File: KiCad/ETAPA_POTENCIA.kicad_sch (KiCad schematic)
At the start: 7 parts, among them U1 LM1117DT-3.3

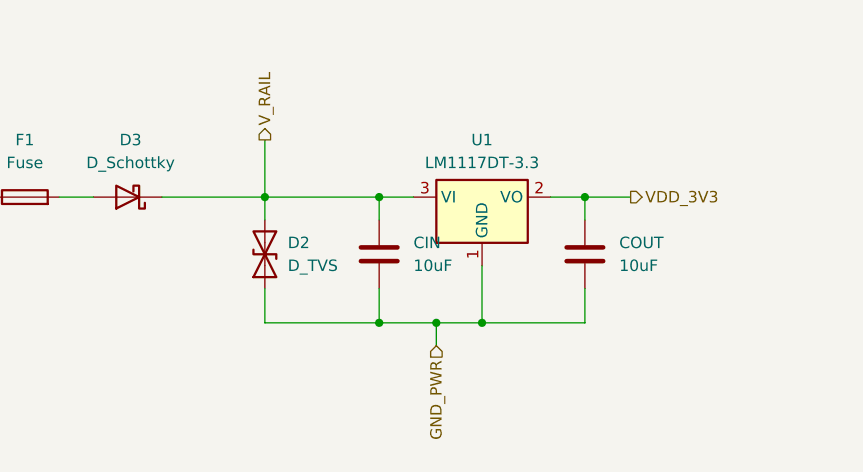
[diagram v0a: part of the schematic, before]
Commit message: Actualització del sensor de corrent
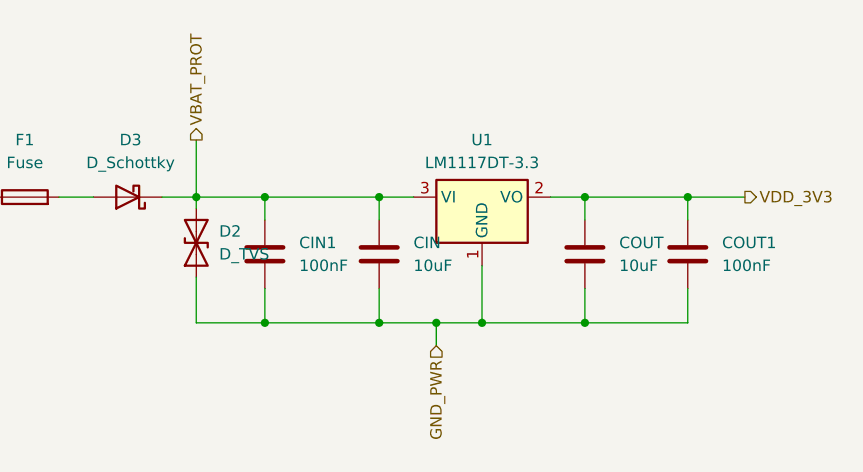
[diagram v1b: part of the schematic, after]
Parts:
- added CIN1, COUT1: 100nF, symbol Device:C
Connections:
- net GND_PWR: now also CIN1.2, COUT1.2
- net VDD_3V3: now also COUT1.1
- net V_RAIL renamed VBAT_PROT
- net VBAT_PROT: now also CIN1.1
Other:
- moved on the sheet: D2

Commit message: Update del micro
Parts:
- added U4: LM2596S-5, Package_TO_SOT_SMD:TO-263-5_TabPin3, symbol Regulator_Switching:LM2596S-5
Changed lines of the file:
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@@
+	)
+	(symbol
+		(lib_id "Regulator_Switching:LM2596S-5")
+		(at 63.5 53.34 0)
+		(unit 1)
+		(exclude_from_sim no)
+		(in_bom yes)
+		(on_board yes)
+		(dnp no)
+		(fields_autoplaced yes)
+		(property "Reference" "U4"
+			(at 63.5 43.18 0)
+			(effects
+				(font
+					(size 1.27 1.27)
+				)
+			)
+		)
+		(property "Value" "LM2596S-5"
+			(at 63.5 45.72 0)
+			(effects
+				(font
+					(size 1.27 1.27)
+				)
+			)
+		)
+		(property "Footprint" "Package_TO_SOT_SMD:TO-263-5_TabPin3"
+			(at 64.77 59.69 0)
+			(effects
+				(font
+					(size 1.27 1.27)
+					(italic yes)
+				)
+				(justify left)
+				(hide yes)
+			)
+		)
+		(property "Datasheet" "http://www.ti.com/lit/ds/symlink/lm2596.pdf"
+			(at 63.5 53.34 0)
+			(effects
+				(font
+					(size 1.27 1.27)
+				)
+				(hide yes)
+			)
+		)
+		(property "Description" "5V 3A Step-Down Voltage Regulator, TO-263"
+			(at 63.5 53.34 0)
+			(effects
+				(font
+					(size 1.27 1.27)
+				)
+				(hide yes)
+			)
+		)
+		(pin "1"
+		)
+		(pin "5"
+		)
+		(pin "3"
+		)
+		(pin "2"
+		)
+		(pin "4"
+		)
+		(instances
+			(project ""
+				(path "/347831db-5db9-4aff-ad32-e56fd770e219/a8709361-50f1-45a9-9990-4a11f8b46576"
+					(reference "U4")
+					(unit 1)
+				)
+			)
+		)
 	)
 	(symbol

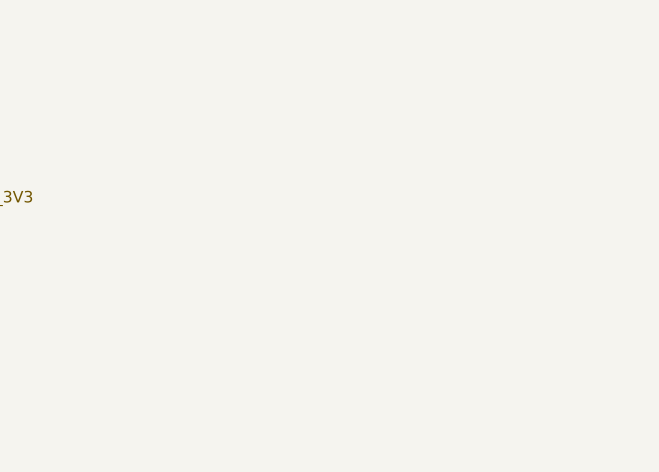
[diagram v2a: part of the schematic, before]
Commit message: BUS CAN + USART +GND comuns
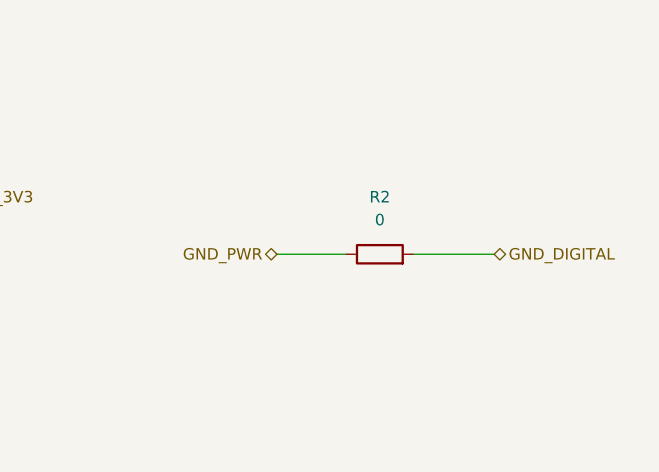
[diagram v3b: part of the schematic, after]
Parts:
- added R2: 0, symbol Device:R
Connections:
- net GND_PWR: now also R2.1
- new net GND_DIGITAL: R2.2
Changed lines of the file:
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@@
+	(wire
+		(pts
+			(xy 196.85 40.64) (xy 205.74 40.64)
+		)
+		(stroke
+			(width 0)
+			(type default)
+		)
+	)
 	(wire
 		(pts
@@
 			(width 0)
 			(type default)
+		)
+	)
+	(wire
+		(pts
+			(xy 181.61 40.64) (xy 189.23 40.64)
+		)
+		(stroke
+			(width 0)
+			(type default)
+		)
+	)
+	(hierarchical_label "GND_DIGITAL"
+		(shape bidirectional)
+		(at 205.74 40.64 0)
+		(effects
+			(font
+				(size 1.27 1.27)
+			)
+			(justify left)
+		)
+	)
+	(hierarchical_label "GND_PWR"
+		(shape bidirectional)
+		(at 181.61 40.64 180)
+		(effects
+			(font
+				(size 1.27 1.27)
+			)
+			(justify right)
 		)
 	)
@@
 					(unit 1)
 				)
+			)
+		)
+	)
+	(symbol
+		(lib_id "Device:R")
+		(at 193.04 40.64 90)
+		(unit 1)
+		(exclude_from_sim no)
+		(in_bom yes)
+		(on_board yes)
+		(dnp no)
+		(fields_autoplaced yes)
+		(property "Reference" "R2"
+			(at 193.04 34.29 90)
+			(effects
+				(font
+					(size 1.27 1.27)
+				)
+			)
+		)
+		(property "Value" "0"
+			(at 193.04 36.83 90)
+			(effects
+				(font
+					(size 1.27 1.27)
+				)
+			)
+		)
+		(property "Footprint" ""
+			(at 193.04 42.418 90)
+			(effects
+				(font
+					(size 1.27 1.27)
+				)
+				(hide yes)
+			)
+		)
+		(property "Datasheet" "~"
+			(at 193.04 40.64 0)
+			(effects
+				(font
+					(size 1.27 1.27)
+				)
+				(hide yes)
+			)
+		)
+		(property "Description" "Resistor"
+			(at 193.04 40.64 0)
+			(effects
+				(font
+					(size 1.27 1.27)
+				)
+				(hide yes)
+			)
+		)
+		(pin "2"
+		)
+		(pin "1"
+		)
+		(instances
+			(project ""
+				(path "/347831db-5db9-4aff-ad32-e56fd770e219/a8709361-50f1-45a9-9990-4a11f8b46576"
+					(reference "R2")
+					(unit 1)
+				)

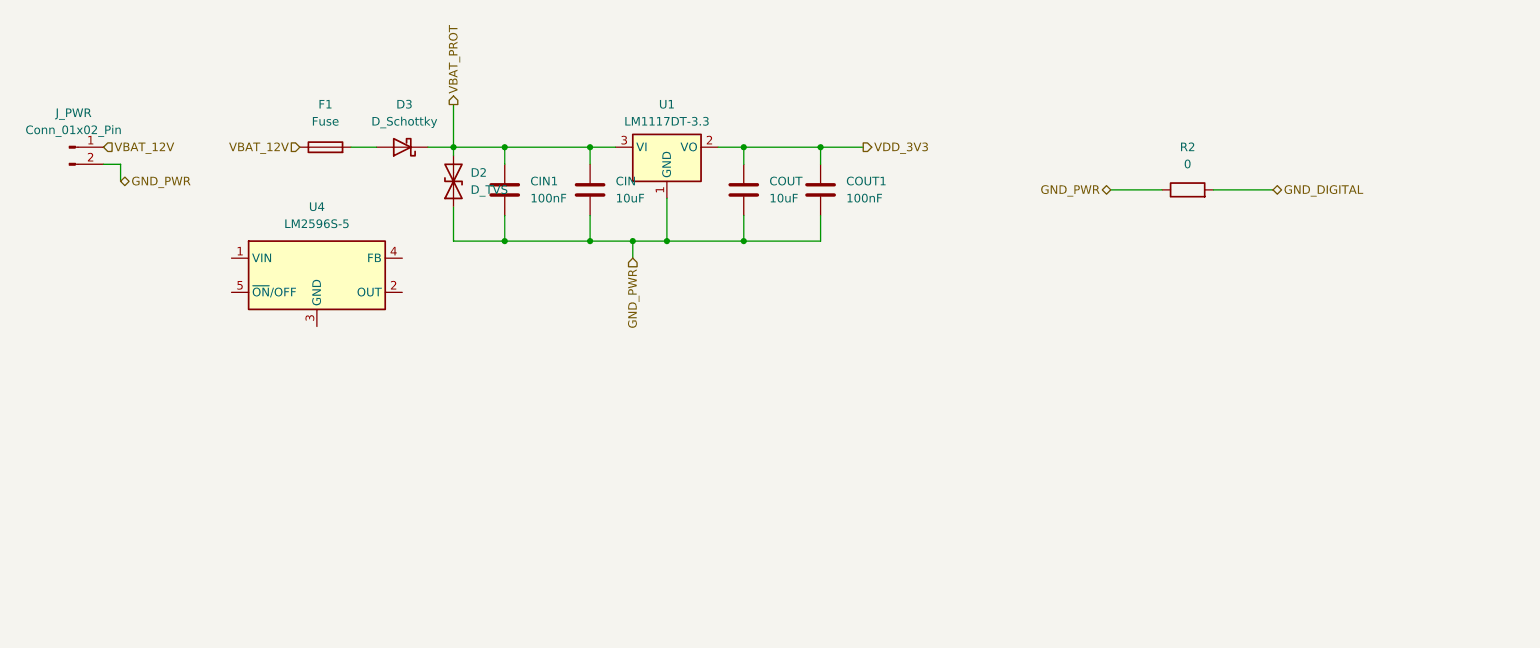
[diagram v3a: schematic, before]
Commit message: Actulització etapa d'alimentació
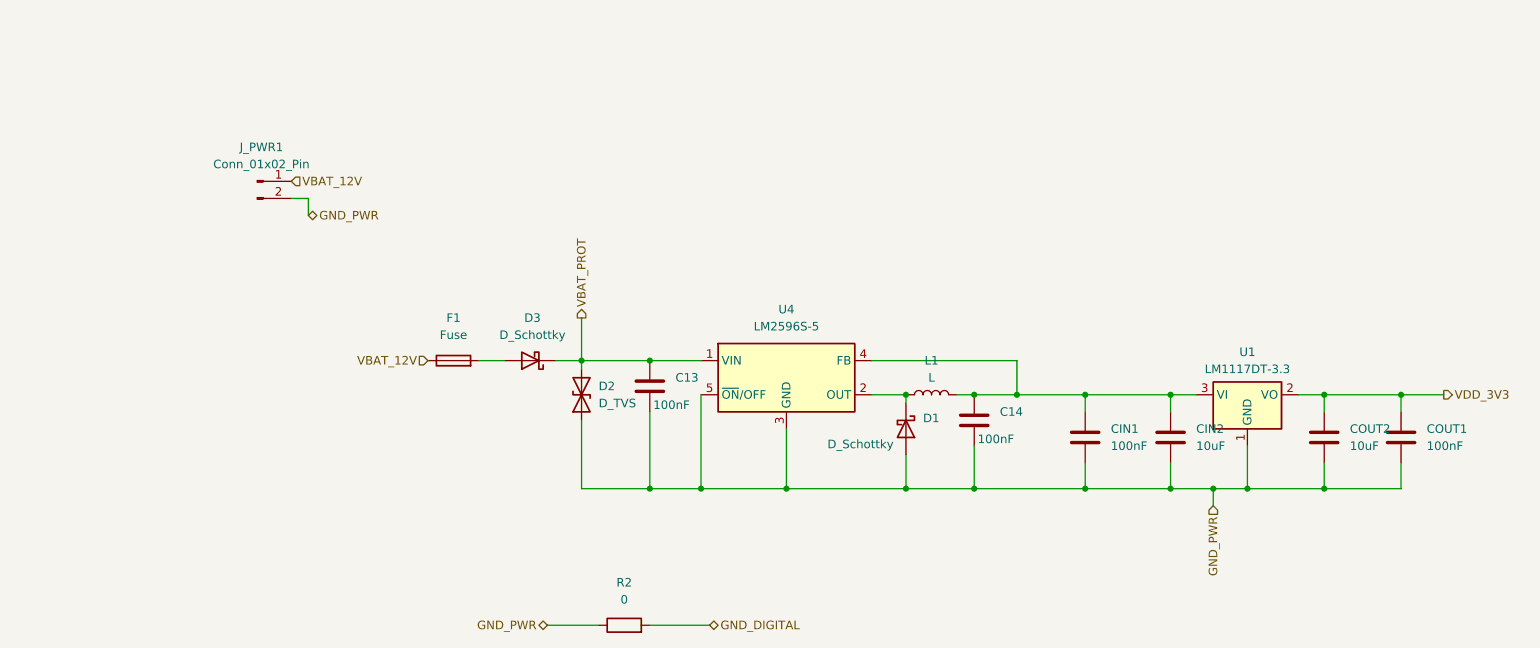
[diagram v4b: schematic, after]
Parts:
- added C13, C14: 100nF, symbol Device:C
- added D1: D_Schottky, symbol Device:D_Schottky
- added L1: L, symbol Device:L
- renumbered CIN to CIN2, COUT to COUT2, J_PWR to J_PWR1
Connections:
- net GND_PWR: now also U4.3 (GND), U4.5 (~{ON}/OFF), C13.2, C14.2, D1.2 (A)
- net VBAT_PROT: now also U4.1 (VIN), C13.1; no longer CIN1.1, CIN2.1, U1.3 (VI)
- net at U4.2 (OUT): now also D1.1 (K), L1.1
- net at U4.4 (FB): now also CIN1.1, CIN2.1, U1.3 (VI), C14.1, L1.2
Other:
- moved on the sheet: CIN1, CIN2, COUT1, COUT2, D2, D3, F1, J_PWR1, R2, U1, U4

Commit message: Actualització README
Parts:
- removed R2: 0, symbol Device:R
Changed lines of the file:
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@@
-	(wire
-		(pts
-			(xy 113.03 105.41) (xy 121.92 105.41)
-		)
-		(stroke
-			(width 0)
-			(type default)
-		)
-	)
 	(wire
 		(pts
@@
 	(wire
 		(pts
-			(xy 97.79 105.41) (xy 105.41 105.41)
-		)
-		(stroke
-			(width 0)
-			(type default)
-		)
-	)
-	(wire
-		(pts
 			(xy 133.35 85.09) (xy 151.13 85.09)
 		)
@@
 			(width 0)
 			(type default)
-		)
-	)
-	(hierarchical_label "GND_DIGITAL"
-		(shape bidirectional)
-		(at 121.92 105.41 0)
-		(effects
-			(font
-				(size 1.27 1.27)
-			)
-			(justify left)
-		)
-	)
-	(hierarchical_label "GND_PWR"
-		(shape bidirectional)
-		(at 97.79 105.41 180)
-		(effects
-			(font
-				(size 1.27 1.27)
-			)
-			(justify right)
 		)
 	)
@@
 					(unit 1)
 				)
-			)
-		)
-	)
-	(symbol
-		(lib_id "Device:R")
-		(at 109.22 105.41 90)
-		(unit 1)
-		(exclude_from_sim no)
-		(in_bom yes)
-		(on_board yes)
-		(dnp no)
-		(fields_autoplaced yes)
-		(property "Reference" "R2"
-			(at 109.22 99.06 90)
-			(effects
-				(font
-					(size 1.27 1.27)
-				)
-			)
-		)
-		(property "Value" "0"
-			(at 109.22 101.6 90)
-			(effects
-				(font
-					(size 1.27 1.27)
-				)
-			)
-		)
-		(property "Footprint" ""
-			(at 109.22 107.188 90)
-			(effects
-				(font
-					(size 1.27 1.27)
-				)
-				(hide yes)
-			)
-		)
-		(property "Datasheet" "~"
-			(at 109.22 105.41 0)
-			(effects
-				(font
-					(size 1.27 1.27)
-				)
-				(hide yes)
-			)
-		)
-		(property "Description" "Resistor"
-			(at 109.22 105.41 0)
-			(effects
-				(font
-					(size 1.27 1.27)
-				)
-				(hide yes)
-			)
-		)
-		(pin "2"
-		)
-		(pin "1"
-		)
-		(instances
-			(project ""
-				(path "/347831db-5db9-4aff-ad32-e56fd770e219/a8709361-50f1-45a9-9990-4a11f8b46576"
-					(reference "R2")
-					(unit 1)
-				)

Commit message: Actualització Sheet Inputs
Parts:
- removed J_PWR1: Conn_01x02_Pin, symbol Connector:Conn_01x02_Pin
- L1: value L -> 33uH
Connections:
- net VDD_5V: now reaches C14.1, CIN1.1, CIN2.1, L1.2, U1.3 (VI), U4.4 (FB)
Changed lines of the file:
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@@
-	(wire
-		(pts
-			(xy 59.69 41.91) (xy 62.23 41.91)
-		)
-		(stroke
-			(width 0)
-			(type default)
-		)
-	)
 	(wire
 		(pts
@@
 	(wire
 		(pts
-			(xy 62.23 41.91) (xy 62.23 44.45)
-		)
-		(stroke
-			(width 0)
-			(type default)
-		)
-	)
-	(wire
-		(pts
 			(xy 120.65 71.12) (xy 120.65 85.09)
 		)
@@
 			(width 0)
 			(type default)
+		)
+	)
+	(label "VDD_5V"
+		(at 167.64 66.04 0)
+		(effects
+			(font
+				(size 1.27 1.27)
+			)
+			(justify left bottom)
 		)
 	)
@@
 		)
 	)
-	(hierarchical_label "GND_PWR"
-		(shape bidirectional)
-		(at 62.23 44.45 0)
-		(effects
-			(font
-				(size 1.27 1.27)
-			)
-			(justify left)
-		)
-	)
 	(hierarchical_label "VDD_3V3"
 		(shape output)
@@
 		)
 	)
-	(hierarchical_label "VBAT_12V"
-		(shape input)
-		(at 59.69 39.37 0)
-		(effects
-			(font
-				(size 1.27 1.27)
-			)
-			(justify left)
-		)
-	)
 	(hierarchical_label "VBAT_PROT"
 		(shape output)
@@
 	)
 	(symbol
-		(lib_id "Connector:Conn_01x02_Pin")
-		(at 54.61 39.37 0)
-		(unit 1)
-		(exclude_from_sim no)
-		(in_bom yes)
-		(on_board yes)
-		(dnp no)
-		(fields_autoplaced yes)
-		(property "Reference" "J_PWR1"
-			(at 55.245 34.29 0)
-			(effects
-				(font
-					(size 1.27 1.27)
-				)
-			)
-		)
-		(property "Value" "Conn_01x02_Pin"
-			(at 55.245 36.83 0)
-			(effects
-				(font
-					(size 1.27 1.27)
-				)
-			)
-		)
-		(property "Footprint" ""
-			(at 54.61 39.37 0)
-			(effects
-				(font
-					(size 1.27 1.27)
-				)
-				(hide yes)
-			)
-		)
-		(property "Datasheet" "~"
-			(at 54.61 39.37 0)
-			(effects
-				(font
-					(size 1.27 1.27)
-				)
-				(hide yes)
-			)
-		)
-		(property "Description" "Generic connector, single row, 01x02, script generated"
-			(at 54.61 39.37 0)
-			(effects
-				(font
-					(size 1.27 1.27)
-				)
-				(hide yes)
-			)
-		)
-		(pin "1"
-		)
-		(pin "2"
-		)
-		(instances
-			(project ""
-				(path "/347831db-5db9-4aff-ad32-e56fd770e219/a8709361-50f1-45a9-9990-4a11f8b46576"
-					(reference "J_PWR1")
-					(unit 1)
-				)
-			)
-		)
-	)
-	(symbol
 		(lib_id "Device:D_Schottky")
 		(at 151.13 76.2 270)
@@
 			)
 		)
-		(property "Value" "L"
+		(property "Value" "33uH"
 			(at 154.94 68.58 90)
 			(effects

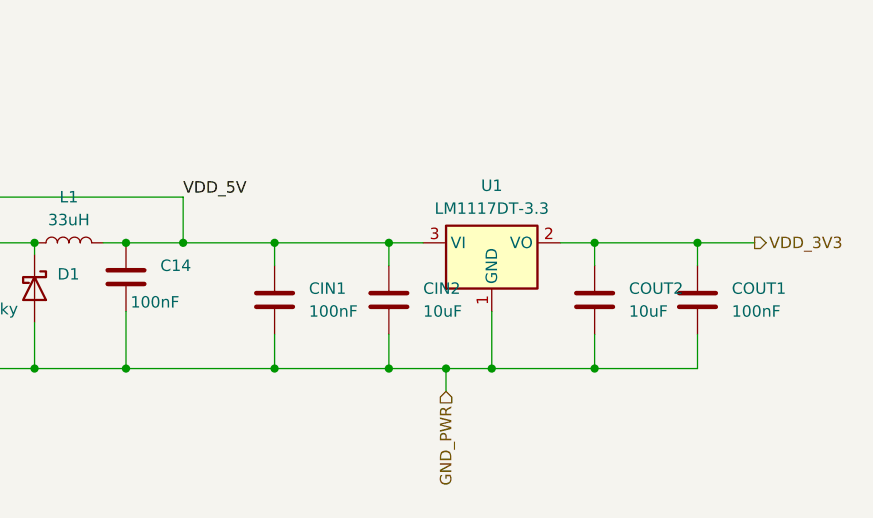
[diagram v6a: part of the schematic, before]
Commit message: Etiquetes de GND i VCC 3.3V canviades a simbols
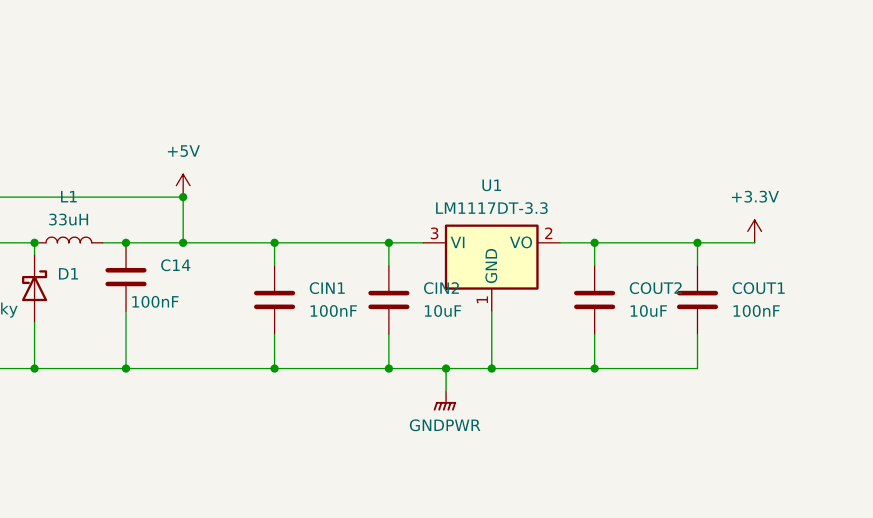
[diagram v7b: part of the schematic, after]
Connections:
- net GND_PWR renamed GNDPWR
- net VDD_3V3 renamed +3.3V
- net VDD_5V renamed +5V
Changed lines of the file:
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@@
+	)
+	(junction
+		(at 167.64 66.04)
+		(diameter 0)
+		(color 0 0 0 0)
 	)
 	(junction
@@
 			(width 0)
 			(type default)
-		)
-	)
-	(label "VDD_5V"
-		(at 167.64 66.04 0)
-		(effects
-			(font
-				(size 1.27 1.27)
-			)
-			(justify left bottom)
-		)
-	)
-	(hierarchical_label "GND_PWR"
-		(shape input)
-		(at 196.85 87.63 270)
-		(effects
-			(font
-				(size 1.27 1.27)
-			)
-			(justify right)
-		)
-	)
-	(hierarchical_label "VDD_3V3"
-		(shape output)
-		(at 231.14 71.12 0)
-		(effects
-			(font
-				(size 1.27 1.27)
-			)
-			(justify left)
 		)
 	)
@@
 	)
 	(symbol
+		(lib_id "power:+3.3V")
+		(at 231.14 71.12 0)
+		(unit 1)
+		(exclude_from_sim no)
+		(in_bom yes)
+		(on_board yes)
+		(dnp no)
+		(fields_autoplaced yes)
+		(property "Reference" "#PWR02"
+			(at 231.14 74.93 0)
+			(effects
+				(font
+					(size 1.27 1.27)
+				)
+				(hide yes)
+			)
+		)
+		(property "Value" "+3.3V"
+			(at 231.14 66.04 0)
+			(effects
+				(font
+					(size 1.27 1.27)
+				)
+			)
+		)
+		(property "Footprint" ""
+			(at 231.14 71.12 0)
+			(effects
+				(font
+					(size 1.27 1.27)
+				)
+				(hide yes)
+			)
+		)
+		(property "Datasheet" ""
+			(at 231.14 71.12 0)
+			(effects
+				(font
+					(size 1.27 1.27)
+				)
+				(hide yes)
+			)
+		)
+		(property "Description" "Power symbol creates a global label with name \"+3.3V\""
+			(at 231.14 71.12 0)
+			(effects
+				(font
+					(size 1.27 1.27)
+				)
+				(hide yes)
+			)
+		)
+		(pin "1"
+		)
+		(instances
+			(project ""
+				(path "/347831db-5db9-4aff-ad32-e56fd770e219/a8709361-50f1-45a9-9990-4a11f8b46576"
+					(reference "#PWR02")
+					(unit 1)
+				)
+			)
+		)
+	)
+	(symbol
 		(lib_id "Device:D_TVS")
 		(at 102.87 71.12 90)
@@
 	)
 	(symbol
+		(lib_id "power:GNDPWR")
+		(at 196.85 87.63 0)
+		(unit 1)
+		(exclude_from_sim no)
+		(in_bom yes)
+		(on_board yes)
+		(dnp no)
+		(fields_autoplaced yes)
+		(property "Reference" "#PWR013"
+			(at 196.85 92.71 0)
+			(effects
+				(font
+					(size 1.27 1.27)
+				)
+				(hide yes)
+			)
+		)
+		(property "Value" "GNDPWR"
+			(at 196.723 91.44 0)
+			(effects
+				(font
+					(size 1.27 1.27)
+				)
+			)
+		)
+		(property "Footprint" ""
+			(at 196.85 88.9 0)
+			(effects
+				(font
+					(size 1.27 1.27)
+				)
+				(hide yes)
+			)
+		)
+		(property "Datasheet" ""
+			(at 196.85 88.9 0)
+			(effects
+				(font
+					(size 1.27 1.27)
+				)
+				(hide yes)
+			)
+		)
+		(property "Description" "Power symbol creates a global label with name \"GNDPWR\" , global ground"
+			(at 196.85 87.63 0)
+			(effects
+				(font
+					(size 1.27 1.27)
+				)
+				(hide yes)
+			)
+		)
+		(pin "1"
+		)
+		(instances
+			(project ""
+				(path "/347831db-5db9-4aff-ad32-e56fd770e219/a8709361-50f1-45a9-9990-4a11f8b46576"
+					(reference "#PWR013")
+					(unit 1)
+				)
+			)
+		)
+	)
+	(symbol
 		(lib_id "Device:D_Schottky")
 		(at 151.13 76.2 270)
@@
 					(unit 1)
 				)
+			)
+		)
+	)
+	(symbol
+		(lib_id "power:+5V")
+		(at 167.64 66.04 0)
+		(unit 1)
+		(exclude_from_sim no)
+		(in_bom yes)
+		(on_board yes)
+		(dnp no)
+		(fields_autoplaced yes)
+		(property "Reference" "#PWR09"
+			(at 167.64 69.85 0)
+			(effects
+				(font
+					(size 1.27 1.27)
+				)
+				(hide yes)
+			)
+		)
+		(property "Value" "+5V"
+			(at 167.64 60.96 0)
+			(effects
+				(font
+					(size 1.27 1.27)
+				)
+			)
+		)
+		(property "Footprint" ""
+			(at 167.64 66.04 0)
+			(effects
+				(font
+					(size 1.27 1.27)
+				)
+				(hide yes)
+			)
+		)
+		(property "Datasheet" ""
+			(at 167.64 66.04 0)
+			(effects
+				(font
+					(size 1.27 1.27)
+				)
+				(hide yes)
+			)
+		)
+		(property "Description" "Power symbol creates a global label with name \"+5V\""
+			(at 167.64 66.04 0)
+			(effects
+				(font
+					(size 1.27 1.27)
+				)
+				(hide yes)
+			)
+		)
+		(pin "1"
+		)
+		(instances
+			(project ""
+				(path "/347831db-5db9-4aff-ad32-e56fd770e219/a8709361-50f1-45a9-9990-4a11f8b46576"
+					(reference "#PWR09")
+					(unit 1)
+				)
